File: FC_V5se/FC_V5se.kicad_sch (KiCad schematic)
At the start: 68 parts, among them IC3 RV-3028-C7_32.768kHz_1ppm_TA_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, J12 USB_C_Receptacle_USB2.0_16P, J16 DEBUG, J18 Payload, J22 SWD Port, J3 Life Makes Lemonade, J5 BM04B-SRSS-TB(LF)(SN), SW1 KMR2, SW2 KMR2, U13 E22-400M30S, U14 TCA4307DGKR, U15 LIS2MDL, U2 ZDSD04GLGEAG, U3 TCA9548APWR, U7 LSM6DSOTR

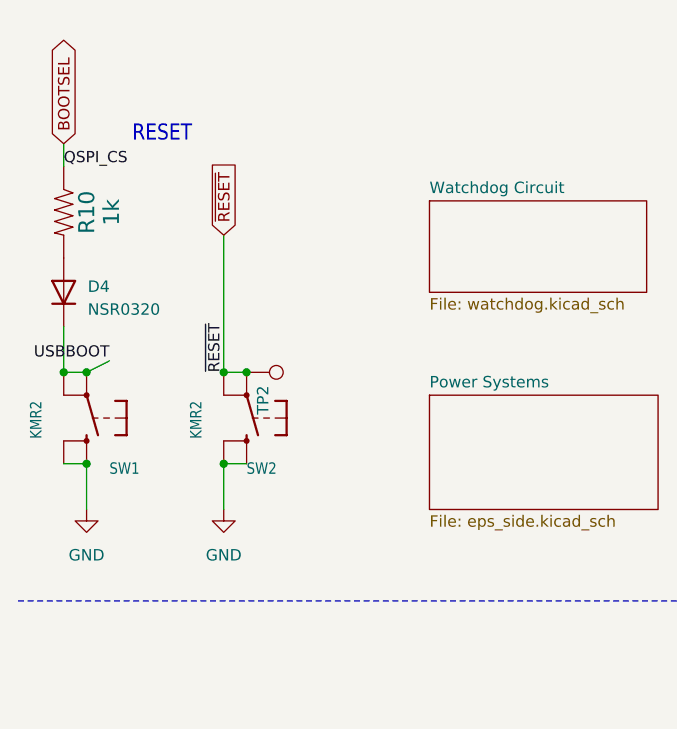
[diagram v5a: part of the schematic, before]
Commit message: V5se: Connected Reset Line to MCU
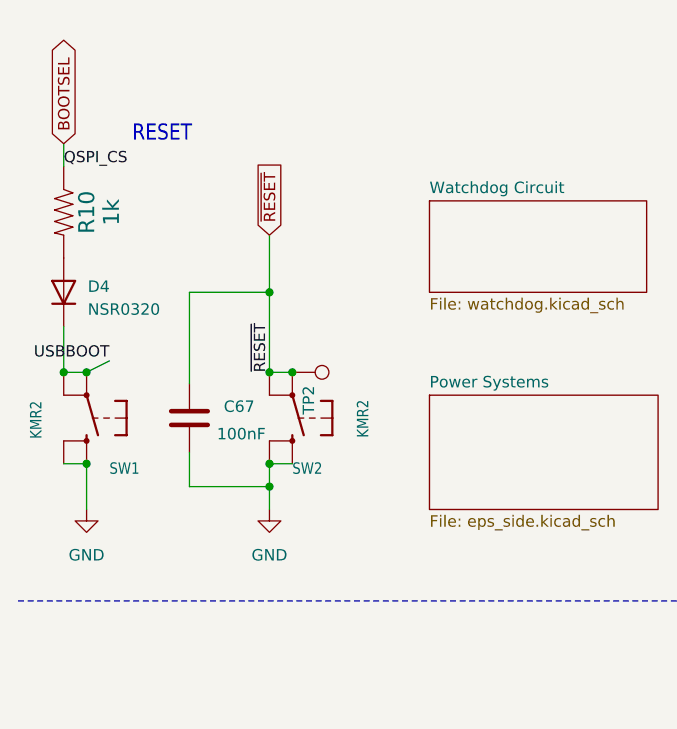
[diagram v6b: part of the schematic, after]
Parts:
- added C67: 100nF, symbol Device:C
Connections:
- net GND: now also C67.2
- net ~{RESET}: now also C67.1
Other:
- moved on the sheet: SW2, TP2
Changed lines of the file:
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@@
 	)
 	(junction
+		(at 39.37 64.77)
+		(diameter 0)
+		(color 0 0 0 0)
+	)
+	(junction
 		(at 251.46 95.25)
 		(diameter 0)
@@
 	)
 	(junction
-		(at 36.83 52.07)
+		(at 41.91 52.07)
 		(diameter 0)
 		(color 0 0 0 0)
@@
 	)
 	(junction
-		(at 34.29 62.23)
+		(at 39.37 62.23)
 		(diameter 0)
 		(color 0 0 0 0)
@@
 	)
 	(junction
-		(at 34.29 52.07)
+		(at 39.37 52.07)
 		(diameter 0)
 		(color 0 0 0 0)
@@
 	)
 	(junction
+		(at 39.37 43.18)
+		(diameter 0)
+		(color 0 0 0 0)
+	)
+	(junction
 		(at 273.05 146.05)
 		(diameter 0)
@@
 	(wire
 		(pts
-			(xy 34.29 36.83) (xy 34.29 52.07)
+			(xy 39.37 36.83) (xy 39.37 43.18)
 		)
 		(stroke
@@
 	(wire
 		(pts
+			(xy 39.37 43.18) (xy 30.48 43.18)
+		)
+		(stroke
+			(width 0)
+			(type default)
+		)
+	)
+	(wire
+		(pts
 			(xy 387.35 217.17) (xy 381 217.17)
 		)
@@
 	(wire
 		(pts
+			(xy 30.48 64.77) (xy 39.37 64.77)
+		)
+		(stroke
+			(width 0)
+			(type default)
+		)
+	)
+	(wire
+		(pts
 			(xy 328.93 115.57) (xy 387.35 115.57)
 		)
@@
 	(wire
 		(pts
+			(xy 30.48 43.18) (xy 30.48 53.34)
+		)
+		(stroke
+			(width 0)
+			(type default)
+		)
+	)
+	(wire
+		(pts
 			(xy 359.41 195.58) (xy 359.41 186.69)
 		)
@@
 	(wire
 		(pts
+			(xy 39.37 43.18) (xy 39.37 52.07)
+		)
+		(stroke
+			(width 0)
+			(type default)
+		)
+	)
+	(wire
+		(pts
 			(xy 138.43 266.7) (xy 138.43 276.86)
 		)
@@
 	(wire
 		(pts
-			(xy 36.83 62.23) (xy 34.29 62.23)
+			(xy 41.91 62.23) (xy 39.37 62.23)
 		)
 		(stroke
@@
 	(wire
 		(pts
-			(xy 34.29 52.07) (xy 36.83 52.07)
+			(xy 39.37 52.07) (xy 41.91 52.07)
 		)
 		(stroke
@@
 	(wire
 		(pts
+			(xy 39.37 64.77) (xy 39.37 62.23)
+		)
+		(stroke
+			(width 0)
+			(type default)
+		)
+	)
+	(wire
+		(pts
 			(xy 287.02 151.13) (xy 287.02 135.89)
 		)
@@
 	(wire
 		(pts
-			(xy 34.29 67.31) (xy 34.29 62.23)
+			(xy 39.37 67.31) (xy 39.37 64.77)
 		)
 		(stroke
@@
 	(wire
 		(pts
+			(xy 30.48 60.96) (xy 30.48 64.77)
+		)
+		(stroke
+			(width 0)
+			(type default)
+		)
+	)
+	(wire
+		(pts
 			(xy 148.59 173.99) (xy 148.59 177.8)
 		)
@@
 	)
 	(label "~{RESET}"
-		(at 34.29 52.07 90)
+		(at 39.37 52.07 90)
 		(effects
 			(font
@@
 	(global_label "~{RESET}"
 		(shape input)
-		(at 34.29 36.83 90)
+		(at 39.37 36.83 90)
 		(fields_autoplaced yes)
 		(effects
@@
 		)
 		(property "Intersheetrefs" "${INTERSHEET_REFS}"
-			(at 34.29 28.0997 90)
+			(at 39.37 28.0997 90)
 			(hide yes)
 			(show_name no)
@@
 	(symbol
 		(lib_id "Adafruit ItsyBitsy RP2040-eagle-import:SWITCH_TACT_SMT4.6X2.8")
-		(at 36.83 57.15 270)
+		(at 41.91 57.15 270)
 		(unit 1)
 		(body_style 1)
@@
 		(dnp no)
 		(property "Reference" "SW2"
-			(at 36.83 63.5 90)
+			(at 41.91 63.5 90)
 			(show_name no)
 			(do_not_autoplace no)
@@
 		)
 		(property "Value" "KMR2"
-			(at 30.48 55.245 0)
+			(at 49.022 55.118 0)
 			(show_name no)
 			(do_not_autoplace no)
@@
 		)
 		(property "Footprint" "FC_DEV_BOARD:BTN_KMR2_4.6X2.8"
-			(at 36.83 57.15 0)
+			(at 41.91 57.15 0)
 			(hide yes)
 			(show_name no)
@@
 		)
 		(property "Datasheet" ""
-			(at 36.83 57.15 0)
+			(at 41.91 57.15 0)
 			(hide yes)
 			(show_name no)
@@
 		)
 		(property "Description" ""
-			(at 36.83 57.15 0)
+			(at 41.91 57.15 0)
 			(hide yes)
 			(show_name no)
@@
 	(symbol
 		(lib_id "Connector:TestPoint")
-		(at 36.83 52.07 270)
+		(at 41.91 52.07 270)
 		(unit 1)
 		(body_style 1)
@@
 		(dnp no)
 		(property "Reference" "TP2"
-			(at 38.6588 53.5432 0)
+			(at 43.7388 53.5432 0)
 			(show_name no)
 			(do_not_autoplace no)
@@
 		)
 		(property "Value" "RESET"
-			(at 37.5158 53.5432 0)
+			(at 42.5958 53.5432 0)
 			(hide yes)
 			(show_name no)
@@
 		)
 		(property "Footprint" "TestPoint:TestPoint_Loop_D1.80mm_Drill1.0mm_Beaded"
-			(at 36.83 57.15 0)
+			(at 41.91 57.15 0)
 			(hide yes)
 			(show_name no)
@@
 		)
 		(property "Datasheet" ""
-			(at 36.83 57.15 0)
+			(at 41.91 57.15 0)
 			(hide yes)
 			(show_name no)
@@
 		)
 		(property "Description" ""
-			(at 36.83 52.07 0)
+			(at 41.91 52.07 0)
 			(hide yes)
 			(show_name no)
@@
 	)
 	(symbol
+		(lib_id "Device:C")
+		(at 30.48 57.15 0)
+		(unit 1)
+		(body_style 1)
+		(exclude_from_sim no)
+		(in_bom yes)
+		(on_board yes)
+		(in_pos_files yes)
+		(dnp no)
+		(property "Reference" "C67"
+			(at 34.29 55.8799 0)
+			(show_name no)
+			(do_not_autoplace no)
+			(effects
+				(font
+					(size 1.27 1.27)
+				)
+				(justify left)
+			)
+		)
+		(property "Value" "100nF"
+			(at 33.528 58.928 0)
+			(show_name no)
+			(do_not_autoplace no)
+			(effects
+				(font
+					(size 1.27 1.27)
+				)
+				(justify left)
+			)
+		)
+		(property "Footprint" ""
+			(at 31.4452 60.96 0)
+			(hide yes)
+			(show_name no)
+			(do_not_autoplace no)
+			(effects
+				(font
+					(size 1.27 1.27)
+				)
+			)
+		)
+		(property "Datasheet" ""
+			(at 30.48 57.15 0)
+			(hide yes)
+			(show_name no)
+			(do_not_autoplace no)
+			(effects
+				(font
+					(size 1.27 1.27)
+				)
+			)
+		)
+		(property "Description" "Unpolarized capacitor"
+			(at 30.48 57.15 0)
+			(hide yes)
+			(show_name no)
+			(do_not_autoplace no)
+			(effects
+				(font
+					(size 1.27 1.27)
+				)
+			)
+		)
+		(pin "2"
+		)
+		(pin "1"
+		)
+		(instances
+			(project "FC_V5se"
+				(path "/c64c0d72-a9f6-4f3a-891e-1f647558f538"
+					(reference "C67")
+					(unit 1)
+				)
+			)
+		)
+	)
+	(symbol
 		(lib_id "mainboard:RESISTOR0603")
 		(at 273.05 138.43 90)
@@
 	(symbol
 		(lib_id "power:GND")
-		(at 34.29 67.31 0)
+		(at 39.37 67.31 0)
 		(unit 1)
 		(body_style 1)
@@
 		(fields_autoplaced yes)
 		(property "Reference" "#PWR021"
-			(at 34.29 73.66 0)
+			(at 39.37 73.66 0)
 			(hide yes)
 			(show_name no)
@@
 		)
 		(property "Value" "GND"
-			(at 34.29 72.39 0)
+			(at 39.37 72.39 0)
 			(show_name no)
 			(do_not_autoplace no)
@@
 		)
 		(property "Footprint" ""
-			(at 34.29 67.31 0)
+			(at 39.37 67.31 0)
 			(hide yes)
 			(show_name no)
@@
 		)
 		(property "Datasheet" ""
-			(at 34.29 67.31 0)
+			(at 39.37 67.31 0)
 			(hide yes)
 			(show_name no)
@@
 		)
 		(property "Description" ""
-			(at 34.29 67.31 0)
+			(at 39.37 67.31 0)
 			(hide yes)
 			(show_name no)
